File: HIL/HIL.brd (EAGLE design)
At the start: 129.6 x 111 mm, 274 parts, among them J1 JTAG_ARM_10PIN, J4 JTAG_ARM_10PIN, M0S0 TPB1,27, M0S1 TPB1,27, M0S2 TPB1,27, M0S3 TPB1,27, M1S0 M0S3, M1S1 M0S3, M1S2 M0S3, M1S3 M0S3, M2S0 M0S3, M2S1 M0S3, M2S2 M0S3, M2S3 M0S3, U1 CD74HC4067SM96, U10 INA219AIDCNR, U11 INA219AIDCNR, U12 INA219AIDCNR, U13 TM4C1294NCPDT, U14 ADUM1201ARZ, U15 SN65HVD230D, U16 TL1963AKTTR., U17 FT230XS, U2 TL1963AKTTR., U3 CD74HC4067SM96, U4 CD74HC4067SM96, U6 TL1963AKTTR., U7 MCP2003-E/SN, U8 DAC7578SPW, U9 INA219AIDCNR, X1 A1944-50, X2 A1944-50, X4 A1944-50, Y3 NX3225GA

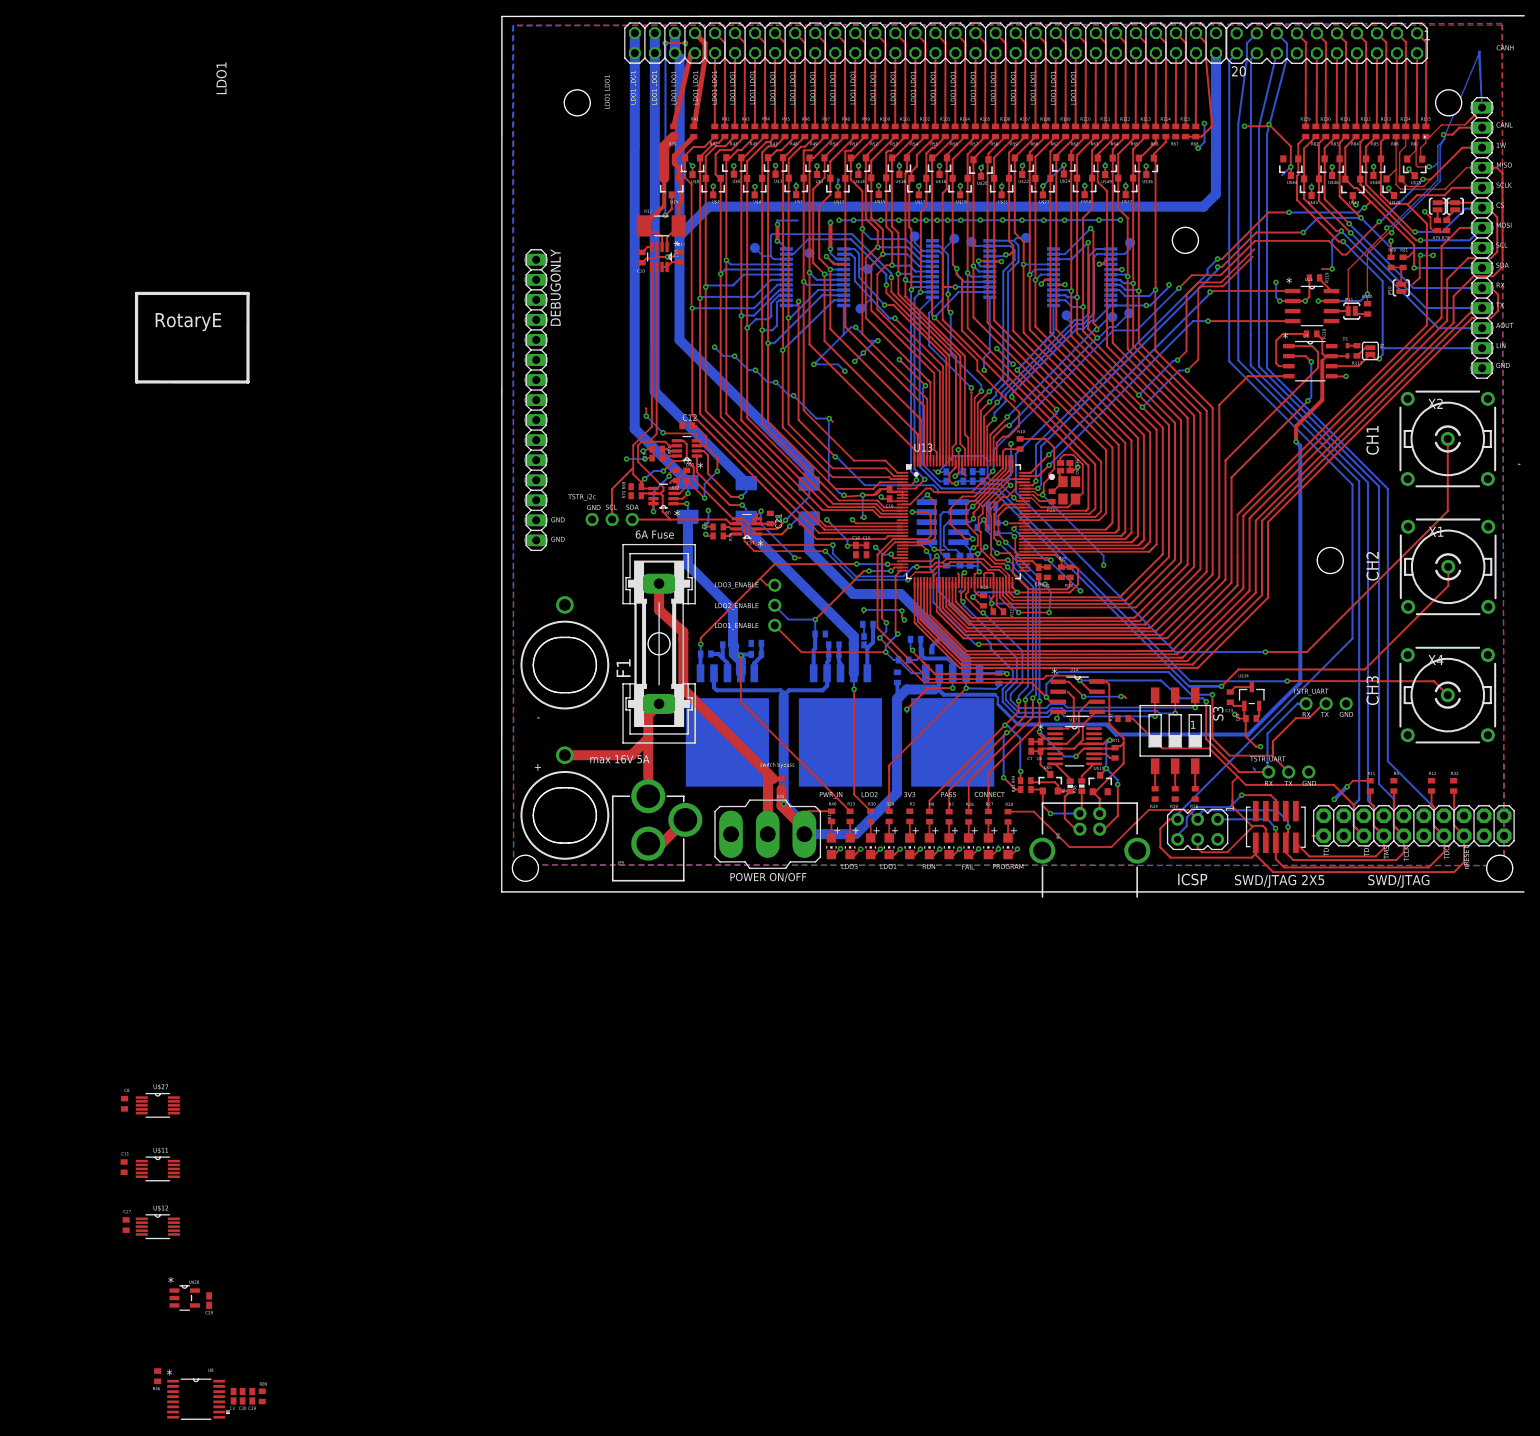
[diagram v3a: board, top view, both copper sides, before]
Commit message: Add: - dac headers          - labels to all the headers
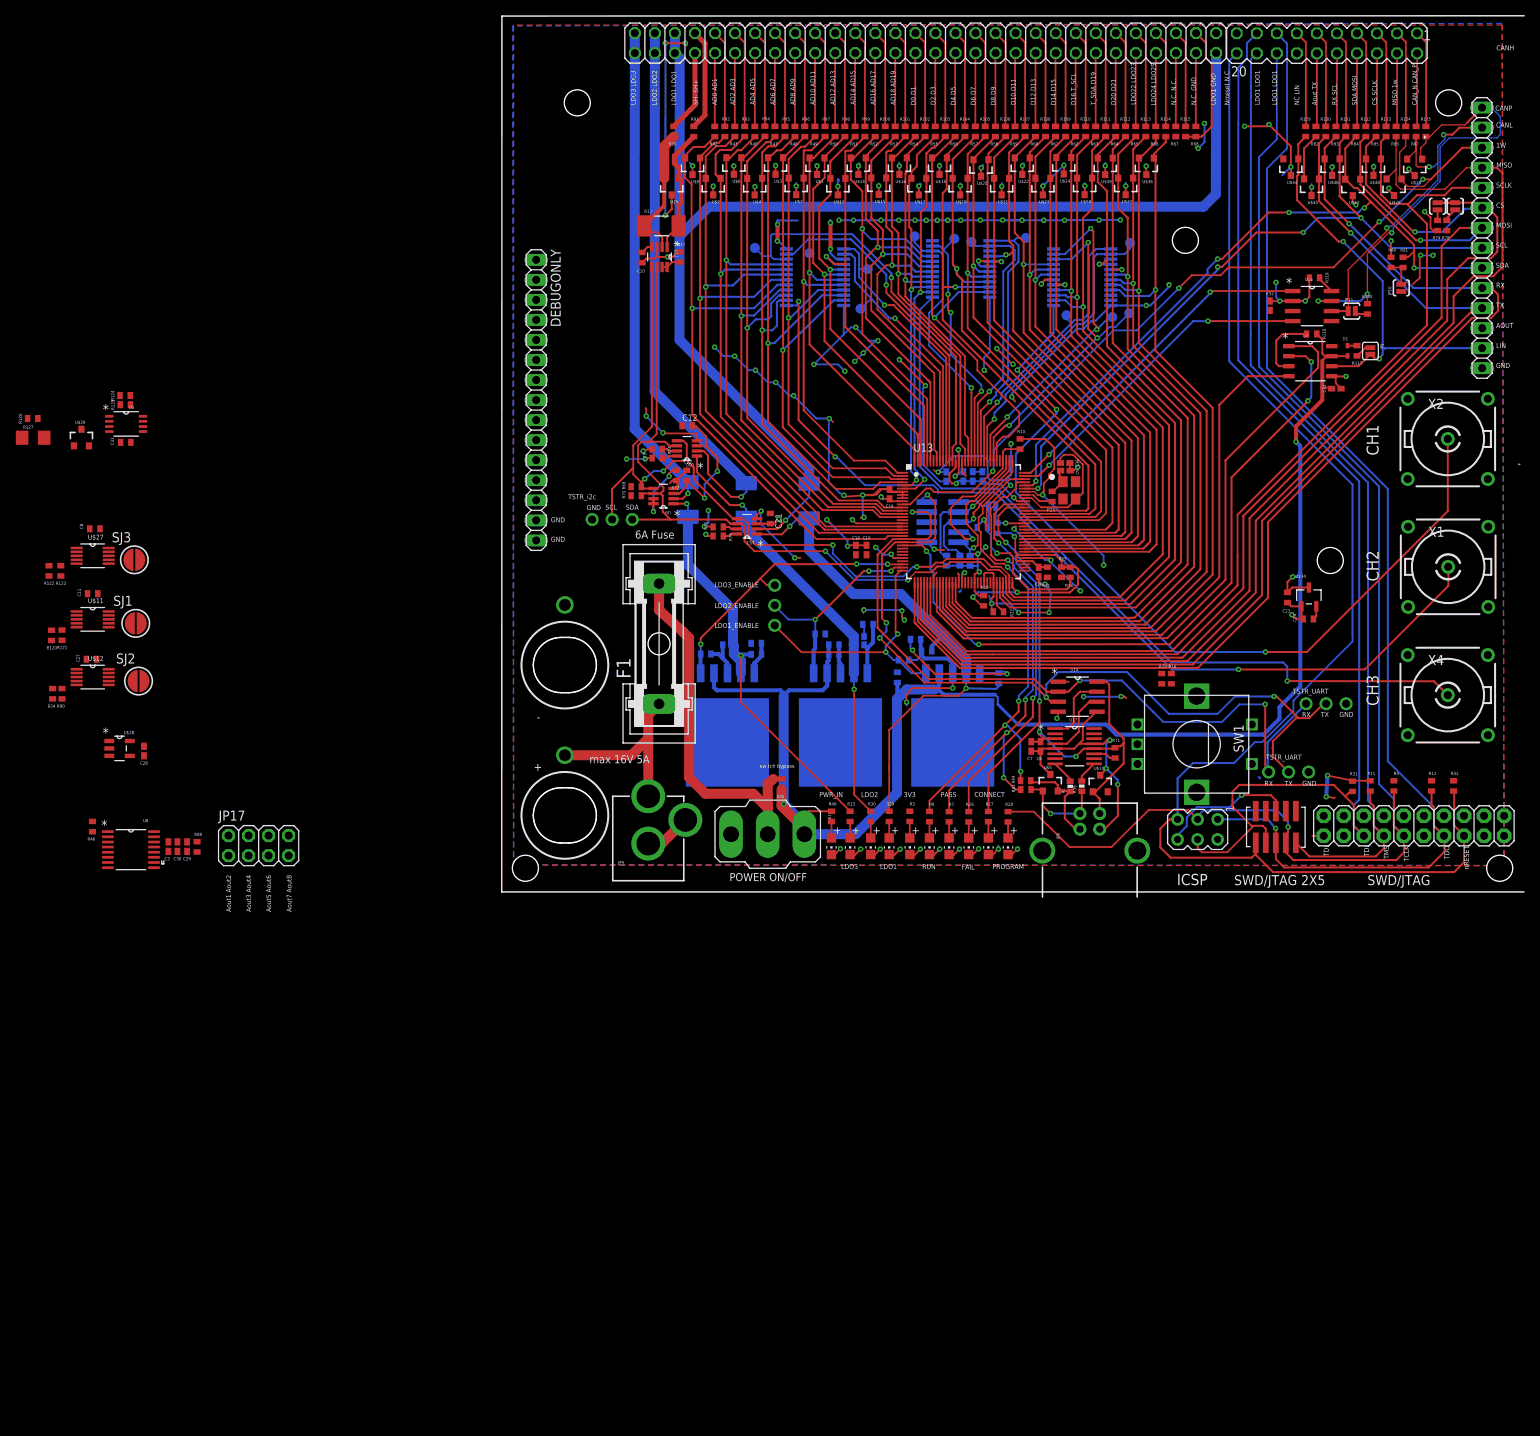
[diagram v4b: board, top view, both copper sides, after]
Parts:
- removed S3: SWS003, smd-special:SMS-003
- added C31: 0.1uF, rcl:C0402
- added C32, C33: 0.1uF 20V, rcl:C0402K
- added JP17: (no value), JDT-1800_smahed:2X04
- added R120, R121, R122, R123, R90: 4k7, resistor:R0402
- added R124: 4k, resistor:R0402
- added R125: 24k, resistor:R0402
- added R126: 10k, resistor:R0402
- added R127: 33k NTC, SparkFun-Passives:1206
- added SJ1, SJ2, SJ3: (no value), SparkFun-Retired:SJ_ROUND
- added SW1: EC12E_SW, switch-alps:ALPS_EC12E_SW
- added U$29: 3v3, SparkFun-DiscreteSemi:SOT23-3
- added U5: MAX11647EUA+T, Maxim_E14:SOP65P490X110-8N
- C23: value 1uF -> 1uF 20V
- R34: value 4.7k -> 4k7
- moved R34 140.3 mm to (-56.9, 25.1)
- moved C8 73.0 mm to (-51.6, 46.0), turned to 180 degrees
- moved C11 72.8 mm to (-51.8, 37.8), turned to 180 degrees
- moved C27 71.8 mm to (-52.0, 29.5), turned to 180 degrees
- moved C28 70.1 mm to (-45.3, 17.9)
- moved C29 70.1 mm to (-39.9, 5.74)
- moved C3 70.1 mm to (-42.2, 5.74)
- moved C30 70.1 mm to (-41.1, 5.74)
- moved R46 70.1 mm to (-51.9, 8.28)
- moved R89 70.1 mm to (-38.6, 5.71)
- moved U$11 70.1 mm to (-49.3, 33.3)
- moved U$12 70.1 mm to (-49.3, 26.0)
- moved U$27 70.1 mm to (-49.3, 41.3)
- moved U$28 70.1 mm to (-48.4, 18.2)
- moved U8 70.1 mm to (-47.0, 5.36)
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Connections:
- removed net N$41: R18.1, S3.6
- removed net N$42: R19.1, S3.5
- removed net N$55: U$11.RH
- removed net N$56: U$11.RW
- removed net N$57: U$11.RL, U$11.V+
- removed net N$67: U$12.RH
- removed net N$68: U$12.RW
- removed net N$69: U$12.RL, U$12.V+
- removed net N$72: U$27.RH
- removed net N$73: U$27.RW
- removed net SW1: S3.3, U13.29
- removed net SW2: S3.2, U13.49
- removed net SW3: S3.1, U13.50
- new net LDO1_RW: SJ1.1, U$11.RW
- new net LDO2_RW: SJ2.1, U$12.RW
- new net LDO3_RW: SJ3.1, U$27.RW
- new net N$82: R19.1, SW1.C
- new net NTC_OUT: R126.1, R127.2, U5.2
- new net ROTARY_A: SW1.A, U13.49
- new net ROTARY_B: SW1.B, U13.50
- new net ROTARY_SW: SW1.D, U13.29
- new net SUPPLY_DIV: R124.1, R125.2, U$29.1, U5.1
- net AOUT_1: now also JP17.1
- net AOUT_2: now also JP17.2
- net AOUT_3: now also JP17.3
- net AOUT_4: now also JP17.4
- net AOUT_5: now also JP17.5
- net AOUT_6: now also JP17.6
- net AOUT_7: now also JP17.7
- net AOUT_8: now also JP17.8
- net GND: now also C31.1, C32.2, C33.1, R120.2, R125.1, R127.1, R90.2, SW1.GND1, SW1.GND2, U$11.RL, U$12.RL, U$27.RL, U$29.2, U5.7
- net LDO1_ADJ: now also SJ1.2
- net LDO1_SH+: now also U$11.RH, U$11.V+
- net LDO2_ADJ: now also SJ2.2
- net LDO2_SH+: now also U$12.RH, U$12.V+
- net LDO3_ADJ: now also SJ3.2
- net N$43: now also R18.1, SW1.E; no longer R34.1, S3.4
- net N$53: now also R120.1
- net N$54: now also R121.1
- net N$63: now also R34.1
- net N$66: now also R90.1
- net N$70: now also R122.1
- net N$71: now also R123.1
- net N$74: now also U$27.RH; no longer U$27.RL
- net POWER_IN_12V: now also C33.2, R124.2
- net TSTR_3V3: now also C31.2, C32.1, R121.2, R122.2, R123.2, R126.2, U5.4, U5.8
- net TSTR_SCL: now also U5.5
- net TSTR_SDA: now also U5.6
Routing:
- net SW1: track 50.9 -> 0.00 mm, vias 2 -> 0
- net SW3: track 44.5 -> 0.00 mm, vias 2 -> 0
- net SW2: track 43.5 -> 0.00 mm, vias 2 -> 0
- net DUT_AOUT1: track 44.4 -> 5.99 mm, vias 2 -> 0
- net TSTR_SCL: track 212.8 -> 185.6 mm, vias 7 -> 5
- net TSTR_SDA: track 209.3 -> 182.8 mm, vias 5 -> 3
- net TDI/MISO: track 168.5 -> 151.6 mm
- net DUT_CAN_P: track 72.2 -> 58.1 mm
- net N$7: track 39.6 -> 46.2 mm
- net CH2: track 125.3 -> 119.4 mm
- net POWER_IN_12V: track 196.0 -> 201.8 mm, vias 2 -> 3
- net NRESET: track 169.9 -> 173.5 mm
- net N$43: track 2.86 -> 0.00 mm
- net N$42: track 2.86 -> 0.00 mm
- net N$41: track 2.86 -> 0.00 mm
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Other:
- outline, holes or cut-outs redrawn
- board text added: "AD0 AD1"
- board text added: "AD10 AD11"
- board text added: "AD12 AD13"
- board text added: "AD14 AD15"
- board text added: "AD16 AD17"
- board text added: "AD18 AD19"
- board text added: "AD2 AD3"
- board text added: "AD4 AD5"
- board text added: "AD6 AD7"
- board text added: "AD8 AD9"
- board text added: "Aout TX"
- board text added: "Aout1 Aout2"
- board text added: "Aout3 Aout4"
- board text added: "Aout5 Aout6"
- board text added: "Aout7 Aout8"
- board text added: "C1"
- board text added: "C10"
- board text added: "C12"
- board text added: "C13"
- board text added: "C14"
- board text added: "C15"
- board text added: "C16"
- board text added: "C17"
- board text added: "C18"
- board text added: "C19"
- board text added: "C2"
- board text added: "C20"
- board text added: "C21"
- board text added: "C22"
- board text added: "C23"
- board text added: "C24"
- board text added: "C25"
- board text added: "C26"
- board text added: "C28"
- board text added: "C29"
- board text added: "C3"
- board text added: "C30"
- board text added: "C36"
- board text added: "C37"
- board text added: "C4"
- board text added: "C5"
- board text added: "C6"
- board text added: "C7"
- board text added: "C9"
- board text added: "CANP"
- board text added: "CAN_N CAN_P"
- board text added: "CS SCLK"
- board text added: "D0 D1"
- board text added: "D1"
- board text added: "D10 D11"
- board text added: "D12 D13"
- board text added: "D14 D15"
- board text added: "D16 T_SCL"
- board text added: "D2 D3"
- board text added: "D20 D21"
- board text added: "D4 D5"
- board text added: "D6 D7"
- board text added: "D8 D9"
- board text added: "DEBUGONLY"
- board text added: "F1"
- board text added: "J4"
- board text added: "JP1"
- board text added: "JP10"
- board text added: "JP11"
- board text added: "JP5"
- board text added: "JP8"
- board text added: "JP9"
- board text added: "LDO1 GND"
- board text added: "LDO2 LDO2"
- board text added: "LDO22 LDO23"
- board text added: "LDO24 LDO25"
- board text added: "LDO3 LDO3"
- board text added: "M0S0"
- board text added: "M0S1"
- board text added: "M0S2"
- board text added: "M0S3"
- board text added: "M1S0"
- board text added: "M1S1"
- board text added: "M1S2"
- board text added: "M1S3"
- board text added: "M2S0"
- board text added: "M2S1"
- board text added: "M2S2"
- board text added: "M2S3"
- board text added: "MISO 1w"
- board text added: "N.C. GND"
- board text added: "N.C. N.C."
- board text added: "NC LIN"
- board text added: "Nrreset N.C."
- board text added: "R1"
- board text added: "R10"
- board text added: "R100"
- board text added: "R101"
- board text added: "R102"
- board text added: "R103"
- board text added: "R104"
- board text added: "R105"
- board text added: "R106"
- board text added: "R107"
- board text added: "R108"
- board text added: "R109"
- board text added: "R11"
- board text added: "R110"
- board text added: "R111"
- board text added: "R112"
- board text added: "R113"
- board text added: "R114"
- board text added: "R115"
- board text added: "R116"
- board text added: "R117"
- board text added: "R118"
- board text added: "R119"
- board text added: "R12"
- board text added: "R129"
- board text added: "R13"
- board text added: "R130"
- board text added: "R131"
- board text added: "R132"
- board text added: "R133"
- board text added: "R134"
- board text added: "R135"
- board text added: "R136"
- board text added: "R137"
- board text added: "R138"
- board text added: "R139"
- board text added: "R14"
- board text added: "R140"
- board text added: "R15"
- board text added: "R16"
- board text added: "R17"
- board text added: "R18"
- board text added: "R19"
- board text added: "R2"
- board text added: "R20"
- board text added: "R21"
- board text added: "R22"
- board text added: "R23"
- board text added: "R24"
- board text added: "R25"
- board text added: "R26"
- board text added: "R27"
- board text added: "R28"
- board text added: "R29"
- board text added: "R3"
- board text added: "R30"
- board text added: "R31"
- board text added: "R32"
- board text added: "R33"
- board text added: "R34"
- board text added: "R35"
- board text added: "R36"
- board text added: "R37"
- board text added: "R38"
- board text added: "R39"
- board text added: "R4"
- board text added: "R40"
- board text added: "R41"
- board text added: "R42"
- board text added: "R43"
- board text added: "R44"
- board text added: "R45"
- board text added: "R46"
- board text added: "R47"
- board text added: "R48"
- board text added: "R49"
- board text added: "R5"
- board text added: "R50"
- board text added: "R51"
- board text added: "R52"
- board text added: "R53"
- board text added: "R54"
- board text added: "R55"
- board text added: "R56"
- board text added: "R57"
- board text added: "R58"
- board text added: "R59"
- board text added: "R6"
- board text added: "R60"
- board text added: "R61"
- board text added: "R62"
- board text added: "R63"
- board text added: "R64"
- board text added: "R65"
- board text added: "R66"
- board text added: "R67"
- board text added: "R68"
- board text added: "R69"
- board text added: "R7"
- board text added: "R70"
- board text added: "R71"
- board text added: "R72"
- board text added: "R73"
- board text added: "R74"
- board text added: "R75"
- board text added: "R76"
- board text added: "R77"
- board text added: "R78"
- board text added: "R79"
- board text added: "R8"
- board text added: "R80"
- board text added: "R81"
- board text added: "R82"
- board text added: "R83"
- board text added: "R84"
- board text added: "R85"
- board text added: "R86"
- board text added: "R87"
- board text added: "R88"
- board text added: "R89"
- board text added: "R9"
- board text added: "R91"
- board text added: "R92"
- board text added: "R93"
- board text added: "R94"
- board text added: "R95"
- board text added: "R96"
- board text added: "R97"
- board text added: "R98"
- board text added: "R99"
- board text added: "RX SCL"
- board text added: "S1"
- board text added: "SDA MOSI"
- board text added: "SH- SH+"
- board text added: "T_SDA D19"
- board text added: "U$1"
- board text added: "U$10"
- board text added: "U$13"
- board text added: "U$14"
- board text added: "U$15"
- board text added: "U$16"
- board text added: "U$17"
- board text added: "U$18"
- board text added: "U$19"
- board text added: "U$2"
- board text added: "U$20"
- board text added: "U$21"
- board text added: "U$22"
- board text added: "U$23"
- board text added: "U$24"
- board text added: "U$25"
- board text added: "U$26"
- board text added: "U$28"
- board text added: "U$3"
- board text added: "U$34"
- board text added: "U$36"
- board text added: "U$37"
- board text added: "U$4"
- board text added: "U$44"
- board text added: "U$45"
- board text added: "U$46"
- board text added: "U$47"
- board text added: "U$48"
- board text added: "U$49"
- board text added: "U$5"
- board text added: "U$50"
- board text added: "U$6"
- board text added: "U$7"
- board text added: "U$8"
- board text added: "U$9"
- board text added: "U1"
- board text added: "U10"
- board text added: "U11"
- board text added: "U12"
- board text added: "U13"
- board text added: "U14"
- board text added: "U15"
- board text added: "U16"
- board text added: "U17"
- board text added: "U2"
- board text added: "U3"
- board text added: "U4"
- board text added: "U6"
- board text added: "U7"
- board text added: "U8"
- board text added: "U9"
- board text added: "X1"
- board text added: "X2"
- board text added: "X4"
- board text removed: "RotaryE"

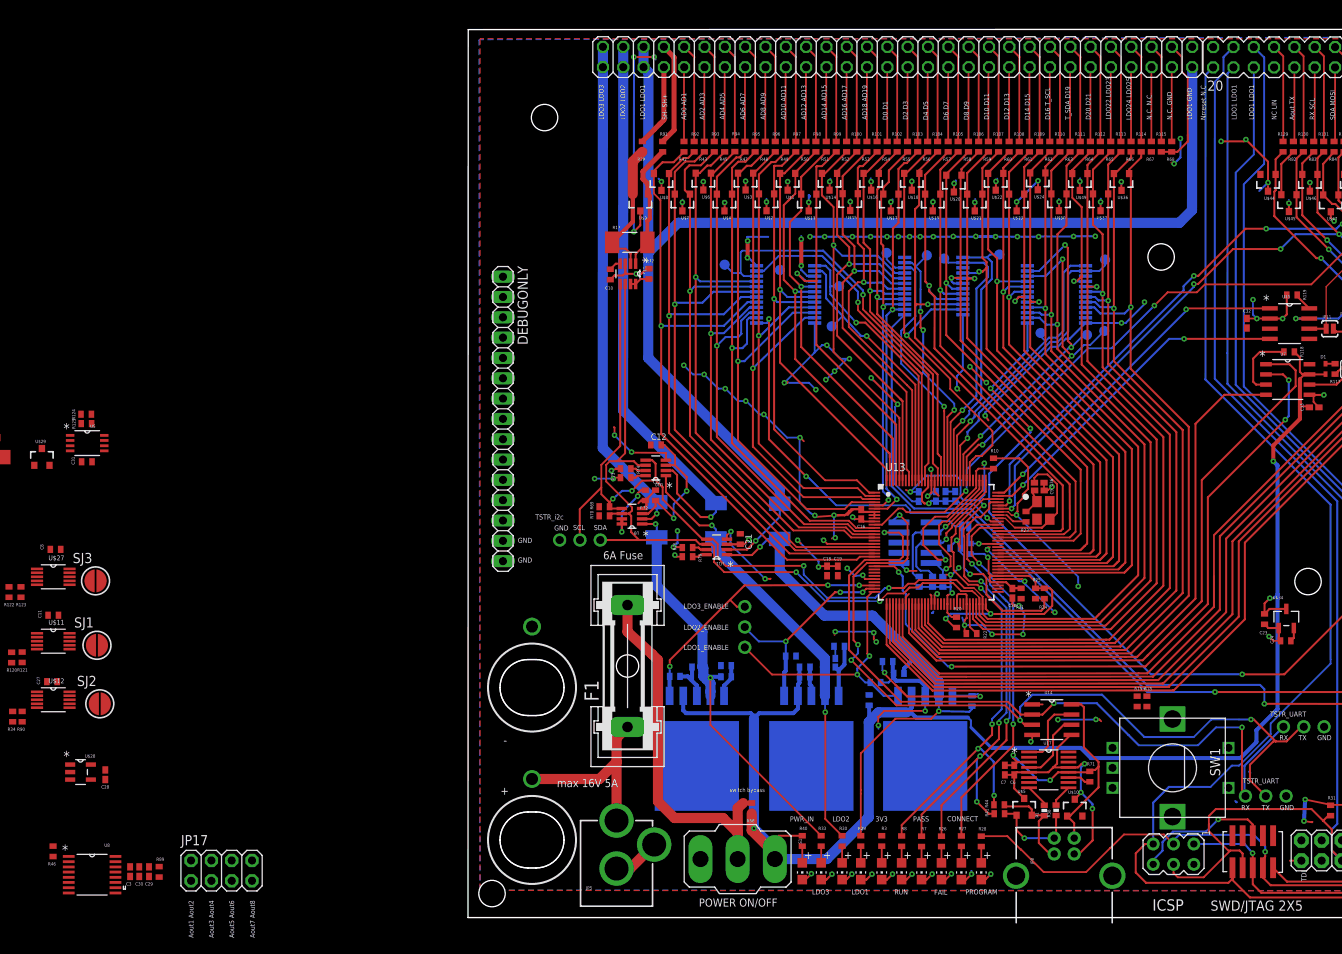
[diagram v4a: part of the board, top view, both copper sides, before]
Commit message: Add DAC layout
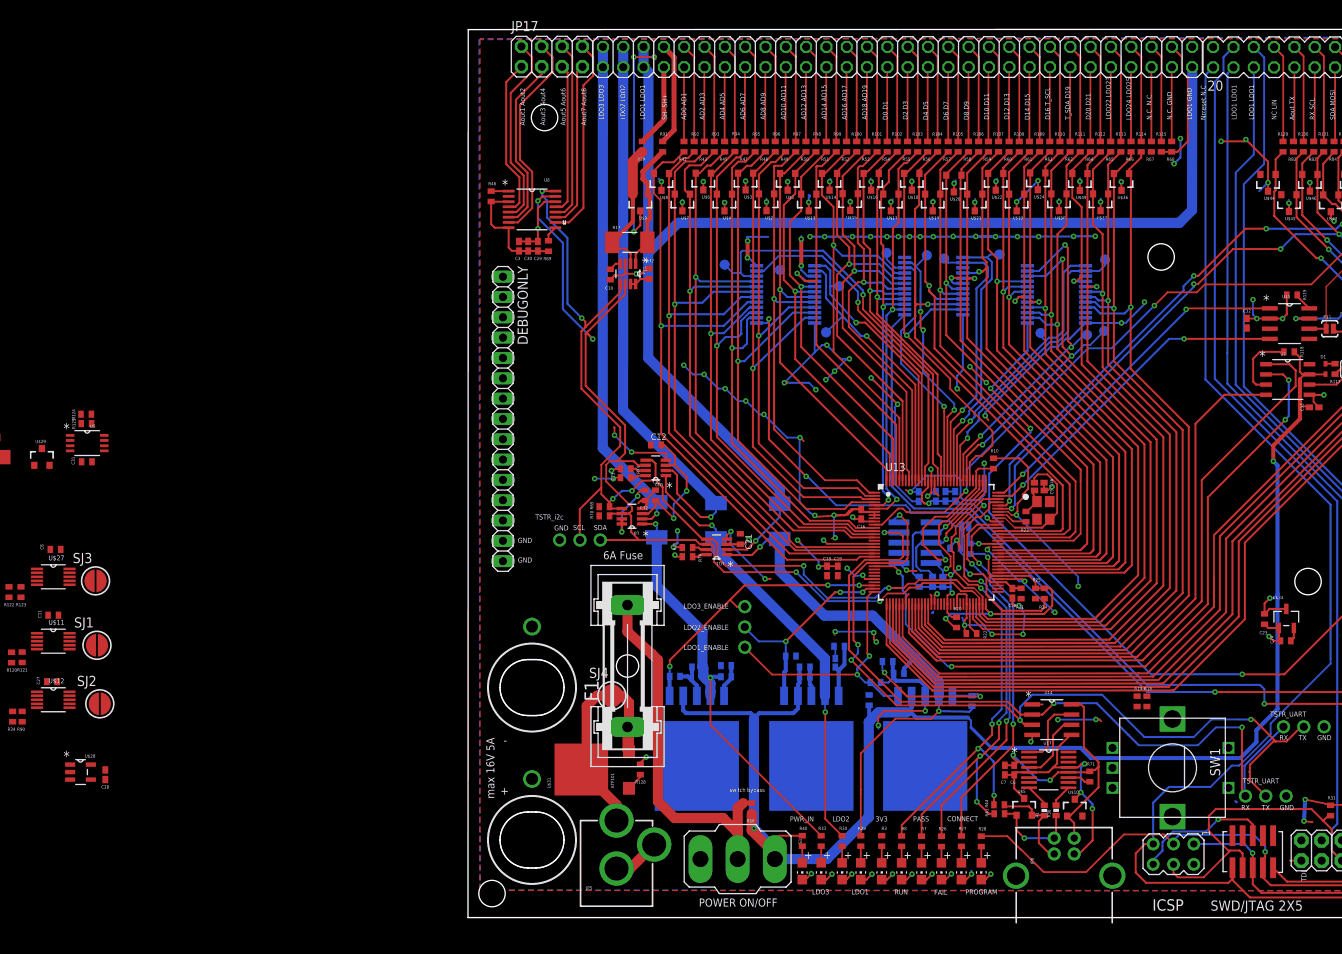
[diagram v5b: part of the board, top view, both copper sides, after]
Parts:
- added R128: 100k, resistor:R0402
- added SJ4: (no value), SparkFun-Retired:SJ_ROUND
- added U$31: ATP101, MosFet_P:ATPACK
- moved JP17 109.8 mm to (10.5, 107.6)
- moved U8 99.7 mm to (8.00, 88.5)
- moved R46 98.5 mm to (2.89, 90.2), turned to 90 degrees
- moved R89 92.1 mm to (10.1, 83.9), turned to 270 degrees
- moved C29 92.1 mm to (8.74, 83.9)
- moved C3 92.1 mm to (6.38, 83.9)
- moved C30 92.1 mm to (7.52, 83.9)
- moved M1S2 1.04 mm to (44.8, 73.2)
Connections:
- removed net DUT_AOUT1: JP3.12, R82.2, U$45.2
- new net N$41: R128.2, U$31.G
- new net VIN_REV: JP12.P$1, JP5.PWR, SJ4.1, U$31.D
- net AOUT_2: now also U8.5; no longer U8.13
- net AOUT_3: now also U8.6; no longer U8.5
- net AOUT_4: now also U8.7; no longer U8.12
- net AOUT_5: now also U8.13; no longer U8.6
- net AOUT_6: now also U8.12; no longer U8.11
- net AOUT_7: now also U8.11; no longer U8.7
- net GND: now also JP3.12, R128.1
- net VIN: now also SJ4.2, U$31.S; no longer JP12.P$1, JP5.PWR
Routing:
- net TSTR_SDA: track 182.8 -> 210.6 mm, vias 3 -> 5
- net AOUT_4: track 0.00 -> 26.8 mm
- net AOUT_8: track 0.00 -> 25.5 mm
- net TSTR_SCL: track 185.6 -> 210.5 mm, vias 5 -> 7
- net AOUT_2: track 0.00 -> 24.3 mm
- net AOUT_6: track 0.00 -> 22.8 mm
- net AOUT_3: track 0.00 -> 22.4 mm
- net AOUT_7: track 0.00 -> 20.9 mm
- net AOUT_1: track 0.00 -> 20.0 mm
- net AOUT_5: track 0.00 -> 18.9 mm
- net VIN_REV: track 0.00 -> 18.8 mm
- net GND: track 327.2 -> 344.4 mm, vias 82 -> 84
- net N$40: track 0.00 -> 15.1 mm
- net VIN: track 23.7 -> 10.5 mm
- net DUT_AOUT1: track 5.99 -> 0.00 mm
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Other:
- board text added: "HILTester A2.1"
- board text removed: "HILTester A2.0"
